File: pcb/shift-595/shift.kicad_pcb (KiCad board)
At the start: 2 copper layers, 12 parts, among them J1 Conn_01x04, J2 GS2, U1 74LS595

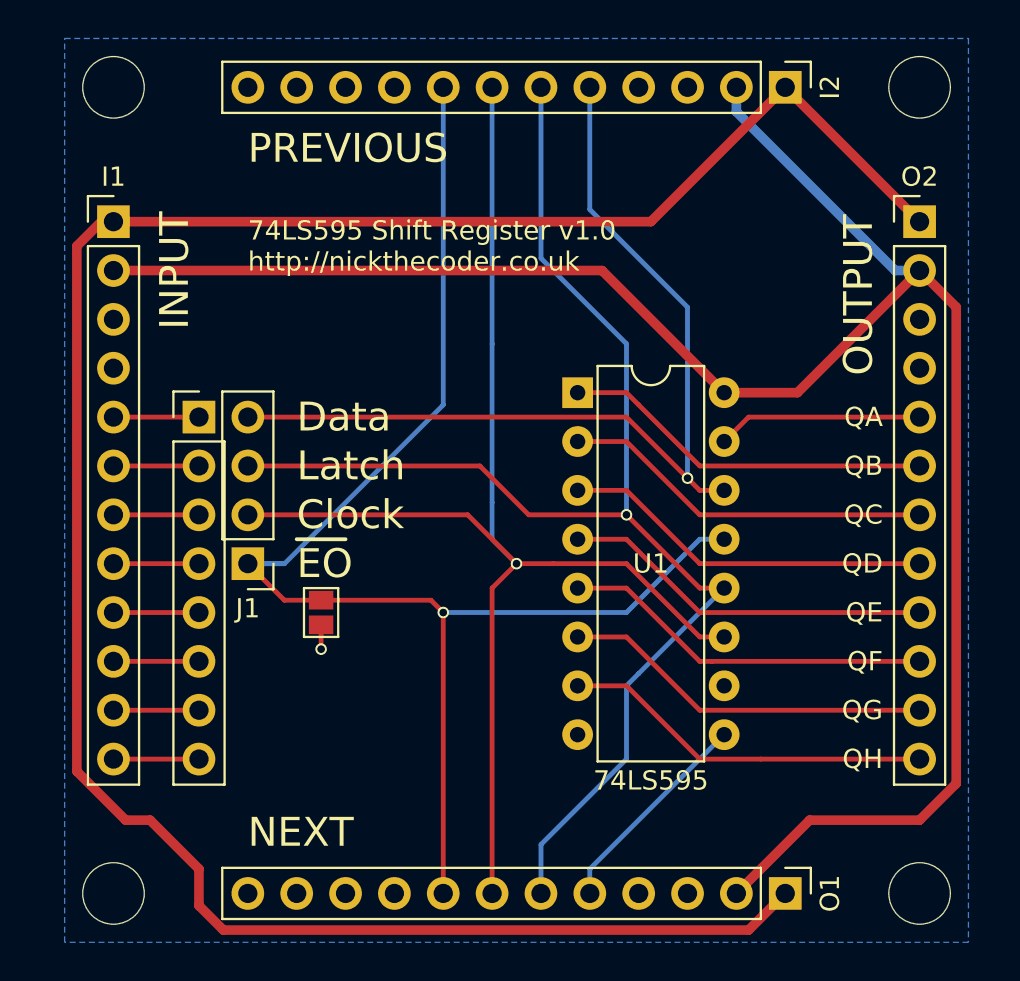
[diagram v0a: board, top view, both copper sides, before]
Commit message: Tweaked shift-595
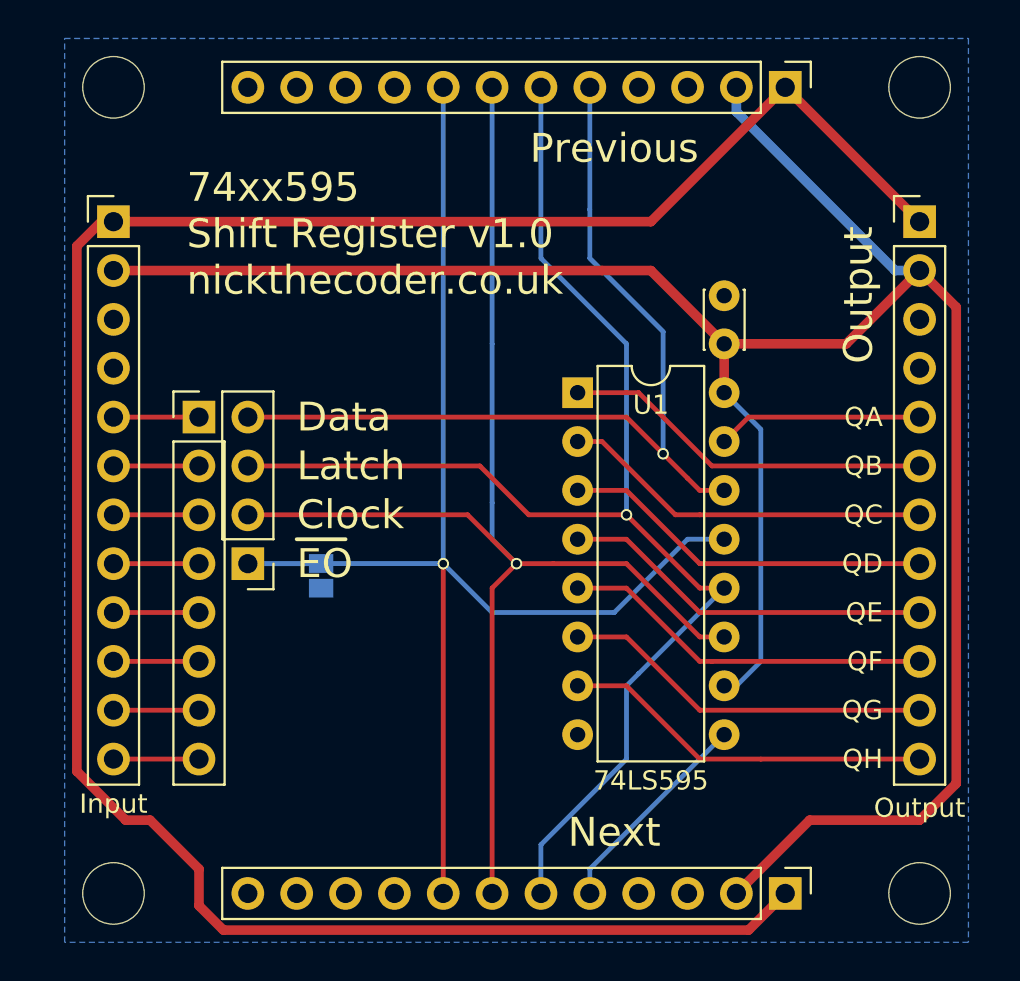
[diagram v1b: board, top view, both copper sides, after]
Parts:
- added C1: C, Capacitors_THT:C_Disc_D3.0mm_W2.0mm_P2.50mm, F.Cu at (160.0, 99.7)
- J1: value Conn_01x04 -> Select
- J2: moved to B.Cu
- moved J2 1.91 mm to (139.1, 111.8), turned to 180 degrees
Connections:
- U1 pad 10: Earth -> VCC
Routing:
- net VCC: track 102.6 -> 120.3 mm
- net /eo: track 74.0 -> 69.3 mm
- net /data: track 48.8 -> 47.0 mm
- net Earth: track 1.26 -> 0.00 mm, vias 1 -> 0
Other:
- board text added: "74xx595 Shift Register v1.0 nickthecoder.co.uk"
- board text added: "Next"
- board text added: "Output"
- board text added: "Previous"
- board text removed: "74LS595 Shift Register v1.0 http://nickthecoder.co.uk"
- board text removed: "INPUT"
- board text removed: "NEXT"
- board text removed: "OUTPUT"
- board text removed: "PREVIOUS"

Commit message: Reworked shift-595 to include 2 banks of outputs (north and south), and the "next" slave is to the east.
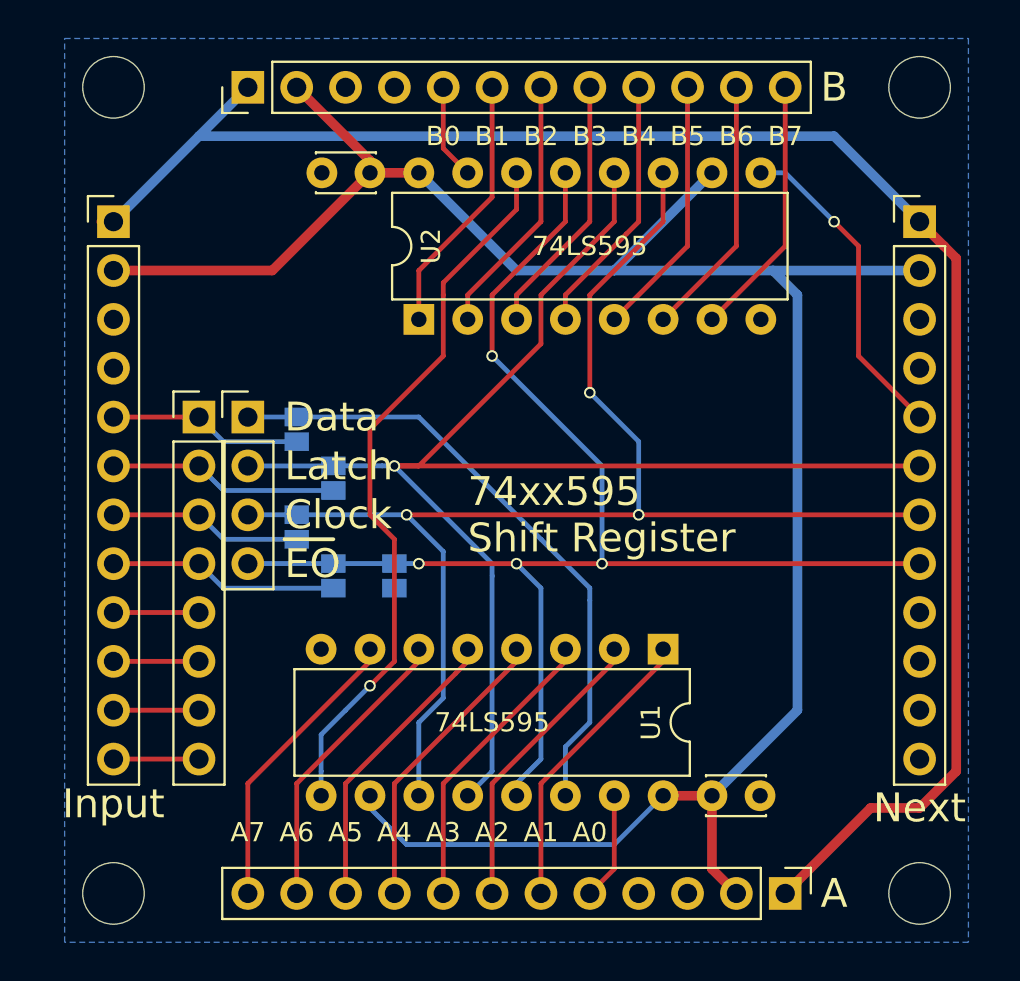
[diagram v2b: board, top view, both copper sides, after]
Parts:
- removed I2: Input, Pin_Headers:Pin_Header_Straight_1x12_Pitch2.54mm
- added C2: C, Capacitors_THT:C_Disc_D3.0mm_W2.0mm_P2.50mm, F.Cu at (141.6, 90.8)
- added J3: GS2, Connectors:GS2, B.Cu at (137.8, 104.1)
- added J4: GS2, Connectors:GS2, B.Cu at (139.7, 106.7)
- added J5: GS2, Connectors:GS2, B.Cu at (137.8, 109.2)
- added J6: GS2, Connectors:GS2, B.Cu at (139.7, 111.8)
- added O3: Output, Socket_Strips:Socket_Strip_Straight_1x12_Pitch2.54mm, F.Cu at (135.3, 86.4)
- added U2: 74LS595, Housings_DIP:DIP-16_W7.62mm, F.Cu at (144.1, 98.4)
- moved O1 35.6 mm to (170.2, 93.3), turned to 0 degrees
- moved O2 35.6 mm to (163.2, 128.3), turned to 270 degrees
- moved C1 23.5 mm to (159.4, 123.2), turned to 0 degrees
- moved U1 14.1 mm to (156.8, 115.6), turned to 270 degrees
- moved J1 7.62 mm to (135.3, 103.5), turned to 0 degrees
- moved J2 3.81 mm to (142.9, 111.8)
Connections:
- net /QA renamed /A0
- net /QB renamed /A1
- net /QC renamed /A2
- net /QD renamed /A3
- net /QE renamed /A4
- net /QF renamed /A5
- net /QG renamed /A6
- net /QH renamed /A7
- net Earth renamed GND
- J1 pad 1: /eo -> /data
- J1 pad 2: /clock -> /latch
- J1 pad 3: /latch -> /clock
- J1 pad 4: /data -> /oe
- J2 pad 1: /eo -> /oe
- O1 pad 8: /eo -> /oe
- U1 pad 13: /eo -> /oe
- U1 pad 9: /next -> Net-(U1-Pad9)
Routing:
- net /oe: track 0.00 -> 72.3 mm, vias 0 -> 4
- net /eo: track 69.3 -> 0.00 mm, vias 1 -> 0
- net Net-(U1-Pad9): track 0.00 -> 37.6 mm, vias 0 -> 1
- net /VIN: track 119.6 -> 90.7 mm
- net /data: track 47.0 -> 32.8 mm, vias 1 -> 0
- net /B7: track 0.00 -> 13.6 mm
- net /B6: track 0.00 -> 13.6 mm
- net /B5: track 0.00 -> 13.6 mm
- net /B4: track 0.00 -> 13.6 mm
- net /B3: track 0.00 -> 13.6 mm
- net /B2: track 0.00 -> 13.6 mm
- net /B1: track 0.00 -> 13.6 mm
- net /L3: track 4.44 -> 12.0 mm
- net /L1: track 4.44 -> 12.0 mm
- net /L2: track 4.44 -> 10.1 mm
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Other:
- board text added: "74xx595 Shift Register"
- board text added: "A"
- board text added: "A0"
- board text added: "A1"
- board text added: "A2"
- board text added: "A3"
- board text added: "A4"
- board text added: "A5"
- board text added: "A6"
- board text added: "A7"
- board text added: "B"
- board text added: "B0"
- board text added: "B1"
- board text added: "B2"
- board text added: "B3"
- board text added: "B4"
- board text added: "B5"
- board text added: "B6"
- board text added: "B7"
- board text added: "Shift 595 v1.0 nickthecoder.co.uk"
- board text added: "Slave : Solder J3,4,5,6 Exclude H1, J1 Master : Solder J2 or include OE of J1"
- board text removed: "74xx595 Shift Register v1.0 nickthecoder.co.uk"
- board text removed: "Output"
- board text removed: "Previous"
- board text removed: "QA"
- board text removed: "QB"
- board text removed: "QC"
- board text removed: "QD"
- board text removed: "QE"
- board text removed: "QF"
- board text removed: "QG"
- board text removed: "QH"
